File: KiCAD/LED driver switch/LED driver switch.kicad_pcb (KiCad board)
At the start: 2 copper layers, 100 x 98 mm, 40 parts, among them J2 3x Banana Jack, J3 Conn_Coaxial, J4 8P8C_Shielded, J5 Conn_01x04_Pin, Q1 PMOS, Q2 TN2124, SW1 SW_Push_LED, U1 Itsy_Bitsy_32u4, U2 4.096V

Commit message: Ordered version
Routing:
- net GND: track 109.1 -> 107.2 mm
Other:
- board text added: "Ballast Resistors"
- board text added: "Door Gnd 5V Audio LED- LED+ LED- LED+"
- board text added: "Gnd SW Green Red Gnd"
- board text added: "Gnd Tx Rx 5V"
- board text removed: "GND SW Green Red Gnd"
- board text removed: "GND TX RX 5V"
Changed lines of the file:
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@@
     (zone_connect 2)
     (attr smd)
-    (fp_text reference "C6" (at -2.47 0) (layer "F.SilkS")
+    (fp_text reference "C6" (at 2.59 -0.07) (layer "F.SilkS")
         (effects (font (size 1 1) (thickness 0.15)))
     )
@@
     (property "Sheetfile" "LED driver switch.kicad_sch")
     (property "Sheetname" "")
+    (zone_connect 2)
     (attr smd)
     (fp_text reference "U2" (at 0.1 2.72 180) (layer "F.SilkS")
@@
     (property "ki_description" "N-MOSFET transistor, gate/source/drain")
     (property "ki_keywords" "transistor NMOS N-MOS N-MOSFET")
+    (zone_connect 2)
     (attr smd)
     (fp_text reference "Q2" (at -3.1 -0.11) (layer "F.SilkS")
@@
     (zone_connect 2)
     (attr smd)
-    (fp_text reference "C5" (at 0 -1.43) (layer "F.SilkS")
+    (fp_text reference "C5" (at 2.535 0.03) (layer "F.SilkS")
         (effects (font (size 1 1) (thickness 0.15)))
     )
@@
     (property "ki_description" "Generic connector, single row, 01x04, script generated")
     (property "ki_keywords" "connector")
+    (zone_connect 2)
     (attr smd)
-    (fp_text reference "J5" (at 0 -6.14) (layer "F.SilkS")
+    (fp_text reference "J5" (at 0.155 -5.9) (layer "F.SilkS")
         (effects (font (size 1 1) (thickness 0.15)))
     )
@@
     (zone_connect 1)
     (attr through_hole)
-    (fp_text reference "C4" (at 0.000001 12.500001 unlocked) (layer "F.SilkS")
+    (fp_text reference "C4" (at -23.571609 -0.412776 unlocked) (layer "F.SilkS")
         (effects (font (size 1 1) (thickness 0.15)))
     )
@@
     (property "ki_keywords" "R network parallel topology isolated")
     (attr exclude_from_pos_files)
-    (fp_text reference "LA1" (at 1.17 2.93) (layer "F.SilkS")
+    (fp_text reference "LA1" (at 0.01 3) (layer "F.SilkS")
         (effects (font (size 1 1) (thickness 0.15)))
     )
@@
     (effects (font (size 3 3) (thickness 0.6) bold) (justify left bottom mirror))
   )
-  (gr_text "-\n\nGnd\n\n\n+" (at 96.71 53.68) (layer "F.SilkS")
+  (gr_text "-\n\nGnd\n\n\n+" (at 97.15 53.65) (layer "F.SilkS")
     (effects (font (size 1.38 1.5) (thickness 0.3) bold) (justify right bottom))
   )
@@
     (effects (font (size 2.2 2) (thickness 0.3)) (justify left bottom))
   )
-  (gr_text "GND\nTX\nRX\n5V" (at 89.985 39.78) (layer "F.SilkS")
-    (effects (font (size 1.5 1.5) (thickness 0.3)) (justify left bottom))
+  (gr_text "Gnd\nTx\nRx\n5V" (at 89.98 40.15) (layer "F.SilkS")
+    (effects (font (size 1.55 1.5) (thickness 0.3)) (justify left bottom))
   )
-  (gr_text "GND\n\nSW\n\nGreen\n\nRed\n\nGnd" (at 68.095 24.51 90) (layer "F.SilkS")
+  (gr_text "Gnd\n\nSW\n\nGreen\n\nRed\n\nGnd" (at 68.095 24.51 90) (layer "F.SilkS")
     (effects (font (size 1.1 1.1) (thickness 0.2) bold) (justify left bottom))
   )
@@
     (effects (font (size 2 2) (thickness 0.3)) (justify left bottom))
   )
+  (gr_text "Door\nGnd\n5V\nAudio\nLED-\nLED+\nLED-\nLED+" (at 38.3 96.93) (layer "F.SilkS")
+    (effects (font (size 1 1) (thickness 0.15)) (justify left bottom))
+  )
+  (gr_text "Ballast Resistors" (at 45.93 104.58) (layer "F.SilkS")
+    (effects (font (size 2 2) (thickness 0.3)))
+  )
   (gr_text "Pushbutton" (at 60.45 18.53) (layer "F.SilkS")
     (effects (font (size 2 2) (thickness 0.3)))
   )
-  (gr_text "RS-232\n" (at 86.865 27.12) (layer "F.SilkS")
+  (gr_text "RS-232\n" (at 86.9 27.51) (layer "F.SilkS")
     (effects (font (size 2 2) (thickness 0.3)))
   )
@@
   (segment (start 61.33505 54.34505) (end 36.175 79.5051) (width 0.5) (layer "F.Cu") (net 2))
   (segment (start 81.025 44.435) (end 80.64 44.82) (width 0.5) (layer "F.Cu") (net 2))
-  (segment (start 36.175 87.55325) (end 36.175 86.345) (width 0.5) (layer "F.Cu") (net 2))
   (segment (start 83.525 44.435) (end 83.525 45.575) (width 0.2) (layer "F.Cu") (net 2))
   (segment (start 51.775 44.915) (end 51.775 45.61) (width 0.2) (layer "F.Cu") (net 2))
@@
   (segment (start 38.53 79.22) (end 64.14 53.61) (width 0.5) (layer "F.Cu") (net 2))
   (segment (start 82.97 46.13) (end 79.91 46.13) (width 0.2) (layer "F.Cu") (net 2))
-  (segment (start 36.175 86.345) (end 36.65 85.87) (width 0.5) (layer "F.Cu") (net 2))
   (segment (start 38.53 82.08) (end 38.53 79.22) (width 0.5) (layer "F.Cu") (net 2))
   (via (at 115.28 55.83) (size 0.8) (drill 0.4) (layers "F.Cu" "B.Cu") (free) (net 2))
@@
   (via (at 99.93 31.69) (size 0.8) (drill 0.4) (layers "F.Cu" "B.Cu") (free) (net 2))
   (via (at 112.48 87.53) (size 0.8) (drill 0.4) (layers "F.Cu" "B.Cu") (free) (net 2))
-  (via (at 114.808 90.71) (size 0.8) (drill 0.4) (layers "F.Cu" "B.Cu") (net 2))
+  (via (at 114.51 90.8) (size 0.8) (drill 0.4) (layers "F.Cu" "B.Cu") (net 2))
   (via (at 66.802 48.26) (size 0.8) (drill 0.4) (layers "F.Cu" "B.Cu") (free) (net 2))
   (via (at 21.33 62.17) (size 0.8) (drill 0.4) (layers "F.Cu" "B.Cu") (free) (net 2))
@@
   (via (at 24.03 51.86) (size 0.8) (drill 0.4) (layers "F.Cu" "B.Cu") (free) (net 2))
   (via (at 52.68 52.74) (size 0.8) (drill 0.4) (layers "F.Cu" "B.Cu") (free) (net 2))
-  (via (at 113.7 89.81) (size 0.8) (drill 0.4) (layers "F.Cu" "B.Cu") (net 2))
+  (via (at 113.46 89.71) (size 0.8) (drill 0.4) (layers "F.Cu" "B.Cu") (net 2))
   (via (at 117.38 43.84) (size 0.8) (drill 0.4) (layers "F.Cu" "B.Cu") (free) (net 2))
   (via (at 67.76 85.99) (size 0.8) (drill 0.4) (layers "F.Cu" "B.Cu") (free) (net 2))
@@
     (polygon
       (pts
-        (xy 117.48002 85.468174)
+        (xy 117.49002 85.258174)
         (xy 116.28 85.47)
         (xy 115.47 85.46)
         (xy 115.5 114.95)
         (xy 120.17 115.17)
-        (xy 120.06 85.47)
+        (xy 120.07 85.26)
       )
     )
@@
         (xy 23.25 94.88)
         (xy 23.21 105.291178)
-        (xy 78.98 105.31)
-        (xy 78.986682 112.600003)
+        (xy 79.42 105.32)
+        (xy 79.426682 112.610003)
         (xy 98.333349 112.623231)
         (xy 116.989969 112.726233)

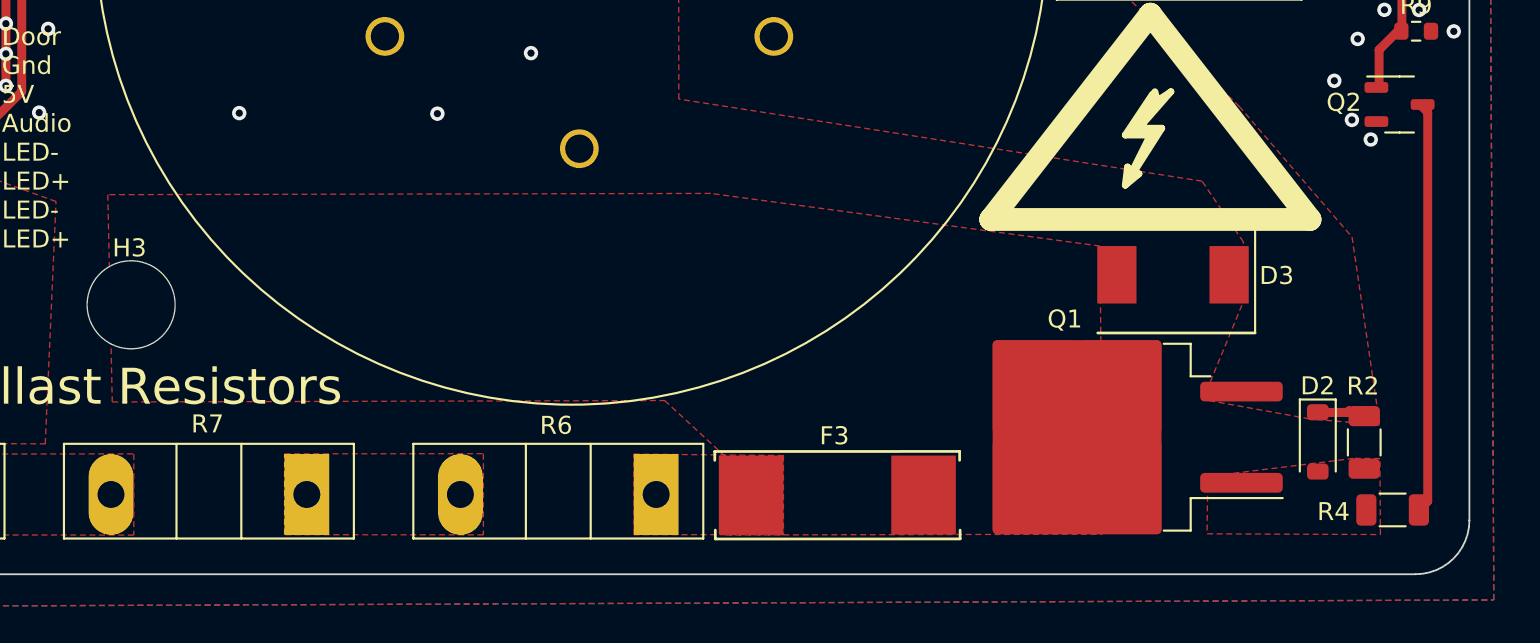
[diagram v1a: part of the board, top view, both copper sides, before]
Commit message: Add HV slots for mosfet
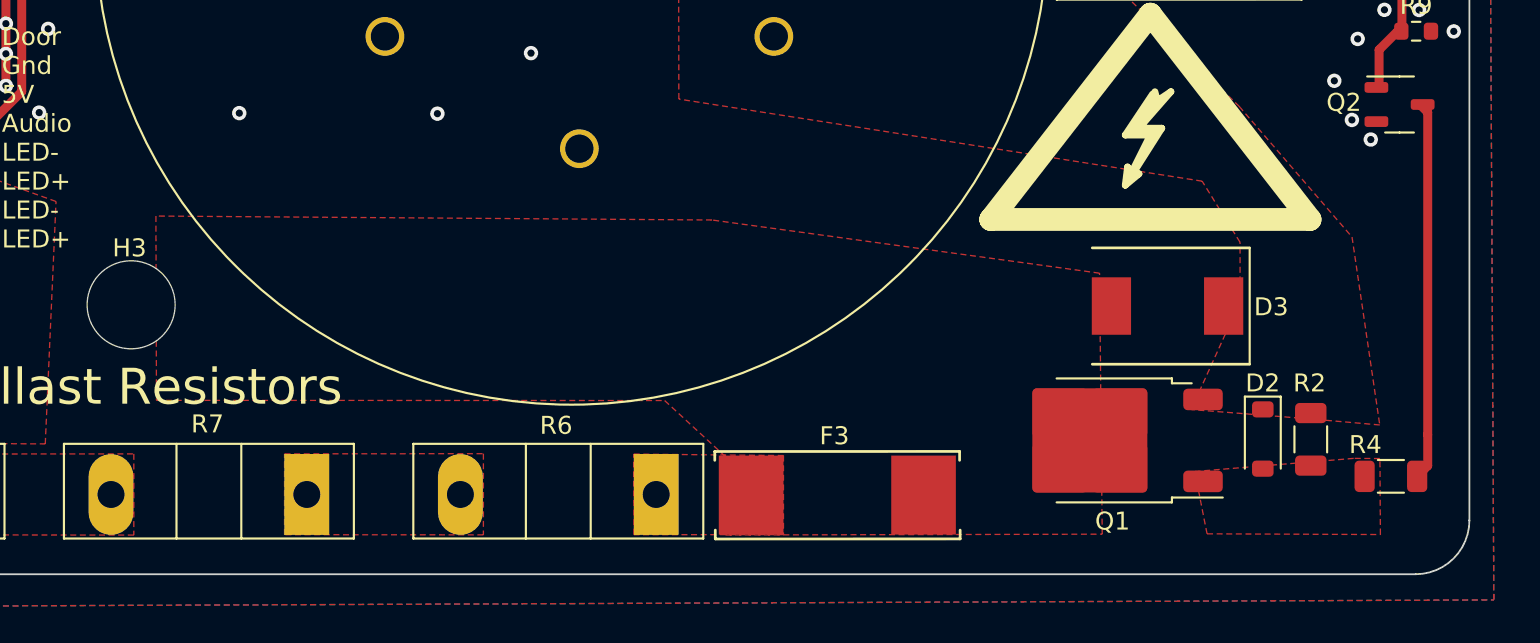
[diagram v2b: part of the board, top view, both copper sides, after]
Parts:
- Q1: footprint Package_TO_SOT_SMD:TO-263-2 -> Custom footprints:TO-252-2 - HV
- R4: footprint Resistor_SMD:R_1206_3216Metric -> Custom footprints:R_1206_3216 - HV slot
- moved D2 3.06 mm to (108.5, 107.5)
- moved R2 2.98 mm to (111.2, 107.5)
- moved R4 1.87 mm to (115.6, 109.5)
- moved D3 1.77 mm to (103.2, 100.1)
- moved Q1 0.50 mm to (100.1, 107.5)
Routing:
- net /0-200V: track 25.9 -> 23.1 mm
- net Net-(Q2-D): track 23.0 -> 21.1 mm

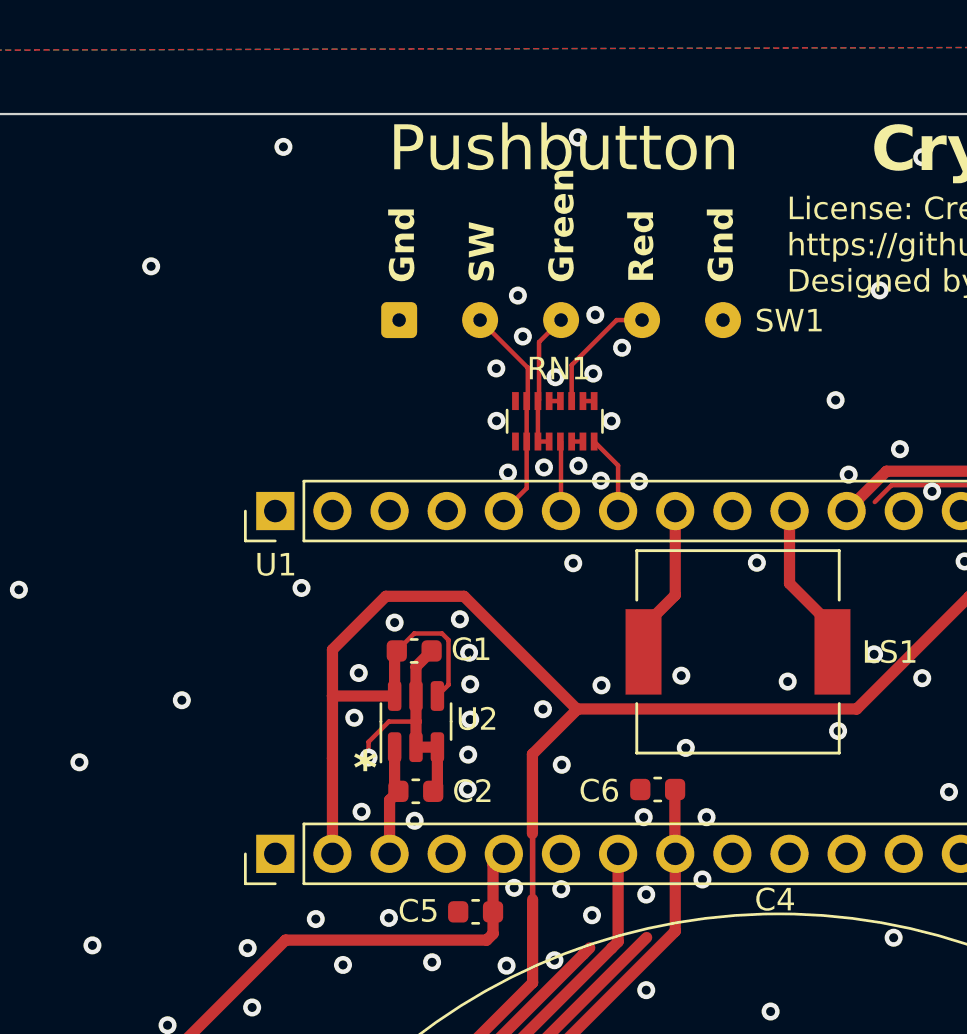
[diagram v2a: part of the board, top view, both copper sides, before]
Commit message: Update PCB to reflect current design
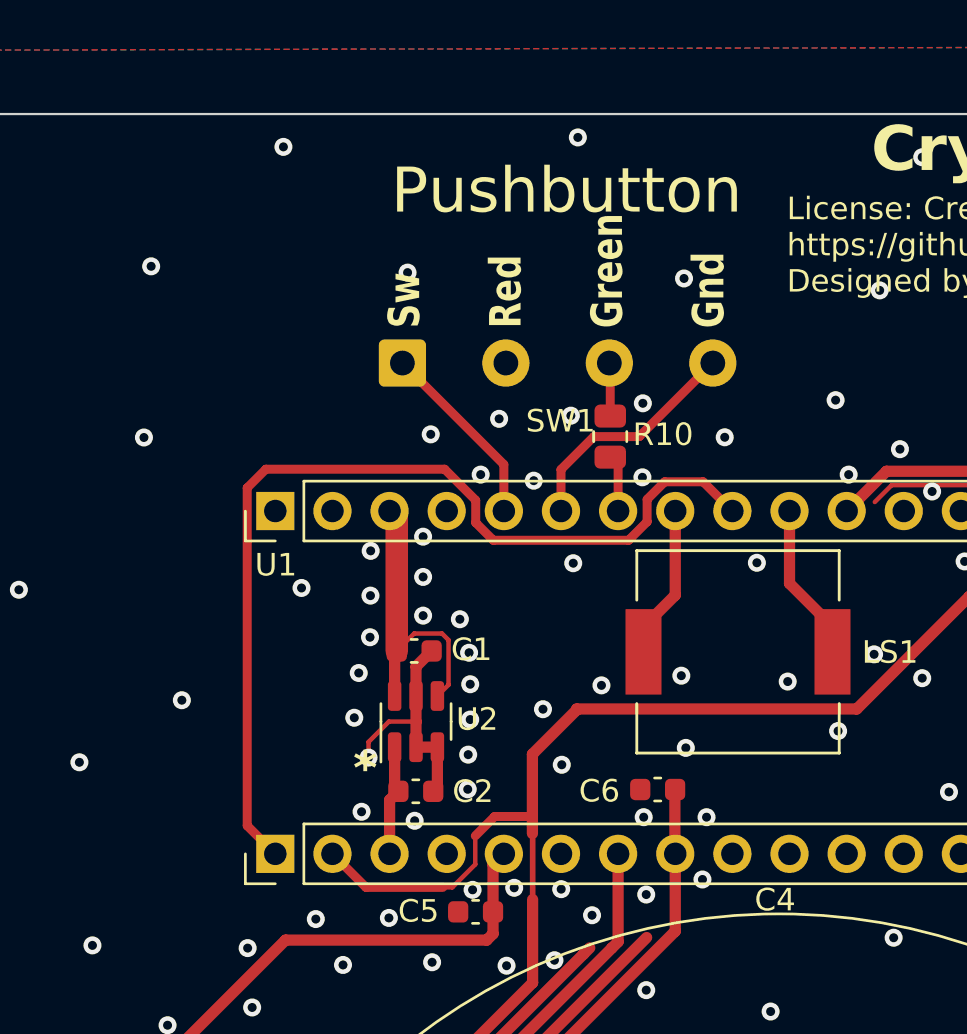
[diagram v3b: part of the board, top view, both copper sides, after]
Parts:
- removed RN1: R_Pack08, Resistor_SMD:R_Array_Convex_8x0602
- added R10: 180, Resistor_SMD:R_0805_2012Metric, F.Cu at (62.5, 31.3)
- SW1: footprint Connector_Wire:SolderWire-0.1sqmm_1x05_P3.6mm_D0.4mm_OD1mm -> Connector_Wire:SolderWire-0.5sqmm_1x04_P4.6mm_D0.9mm_OD2.1mm
- moved SW1 1.92 mm to (53.3, 28.1)
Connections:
- C1 pad 1: +5V -> /Vbus
- SW1 pad 1: GND -> /Pushbutton
- SW1 pad 2: /Pushbutton -> GND
- SW1 pad 4: Net-(RN1-R3.1) -> /Green_LED
- U1 pad 1: unconnected-(U1-Reset-Pad1) -> /reset
- U1 pad 25: unconnected-(U1-7-Pad25) -> /reset
- U1 pad 31: unconnected-(U1-VBus-Pad31) -> /Vbus
- U2 pad 4: +5V -> /Vbus
- U2 pad 6: +5V -> /Vbus
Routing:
- net /reset: track 0.00 -> 42.8 mm
- net +5V: track 121.5 -> 99.8 mm
- net /Vbus: track 0.00 -> 13.8 mm
- net /Green_LED: track 3.10 -> 10.6 mm
- net Net-(RN1-R3.1): track 5.56 -> 0.00 mm
- net Net-(R10-Pad2): track 6.33 -> 2.37 mm
- net /Pushbutton: track 9.81 -> 8.45 mm
- net /Red_LED: track 3.53 -> 2.54 mm
- net Net-(RN1-R4.1): track 0.50 -> 0.00 mm
- net Net-(RN1-R2.2): track 0.50 -> 0.00 mm
- net Net-(RN1-R1.1): track 0.50 -> 0.00 mm
- net GND: vias 198 -> 201
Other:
- board text added: "Sw Red Green Gnd"
- board text removed: "Gnd SW Green Red Gnd"
